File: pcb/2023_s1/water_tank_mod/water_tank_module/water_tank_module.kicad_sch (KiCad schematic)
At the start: 12 parts, among them J1 Conn_01x06_Male, U4 NRF24L01_Breakout

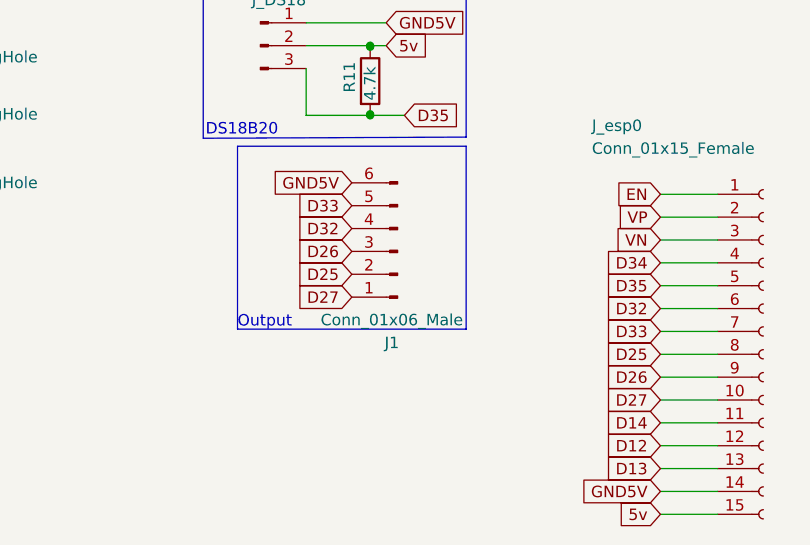
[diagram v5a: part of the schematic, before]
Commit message: fix, separated the light control into another pcb, due to the different voltage it handles and confort for the use
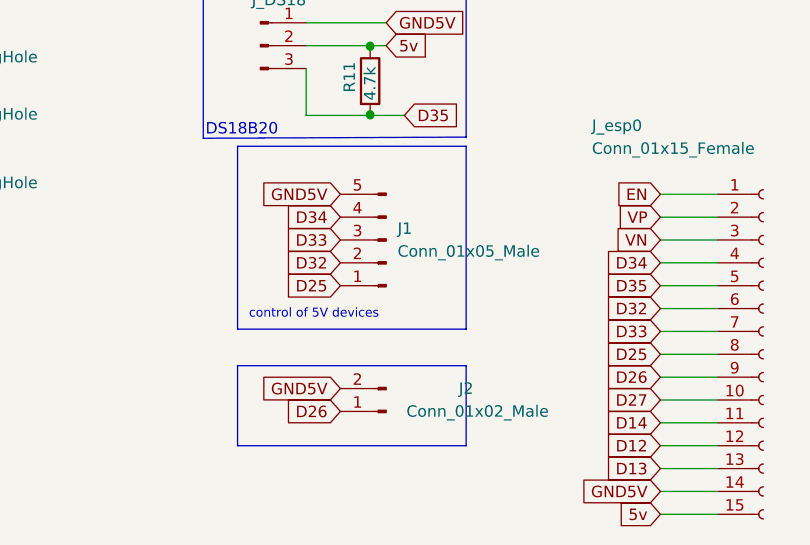
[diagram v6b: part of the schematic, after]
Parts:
- removed J1: Conn_01x06_Male, Connector_JST:JST_EH_B6B-EH-A_1x06_P2.50mm_Vertical, symbol Connector:Conn_01x06_Male
- added J1: Conn_01x05_Male, Connector_JST:JST_EH_B5B-EH-A_1x05_P2.50mm_Vertical, symbol Connector:Conn_01x05_Male
- added J2: Conn_01x02_Male, Connector_JST:JST_EH_B2B-EH-A_1x02_P2.50mm_Vertical, symbol Connector:Conn_01x02_Male
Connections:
- net D25: now also J1.1 (Pin_1)
- net D26: now also J2.1 (Pin_1)
- net D32: now also J1.2 (Pin_2)
- net D33: now also J1.3 (Pin_3)
- net D34: now also J1.4 (Pin_4)
- net GND5V: now also J1.5 (Pin_5), J2.2 (Pin_2)
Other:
- note added: "control of 5V devices"
- note removed: "Output"
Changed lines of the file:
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@@
+    (stroke (width 0) (type default) (color 0 0 0 0))
+  )
+  (polyline (pts (xy 76.2 88.9) (xy 101.6 88.9))
     (stroke (width 0) (type default) (color 0 0 0 0))
   )
@@
     (stroke (width 0) (type default) (color 0 0 0 0))
   )
+  (polyline (pts (xy 76.2 88.9) (xy 76.2 97.79))
+    (stroke (width 0) (type default) (color 0 0 0 0))
+  )
   (wire (pts (xy 123.19 100.33) (xy 129.54 100.33))
     (stroke (width 0) (type default) (color 0 0 0 0))
@@
     (stroke (width 0) (type default) (color 0 0 0 0))
   )
+  (polyline (pts (xy 101.6 88.9) (xy 101.6 97.79))
+    (stroke (width 0) (type default) (color 0 0 0 0))
+  )
   (wire (pts (xy 123.19 92.71) (xy 129.54 92.71))
     (stroke (width 0) (type default) (color 0 0 0 0))
@@
   )
   (wire (pts (xy 143.51 33.02) (xy 143.51 35.56))
+    (stroke (width 0) (type default) (color 0 0 0 0))
+  )
+  (polyline (pts (xy 101.6 97.79) (xy 76.2 97.79))
     (stroke (width 0) (type default) (color 0 0 0 0))
   )
@@
     (effects (font (size 1.27 1.27)) (justify left bottom))
   )
-  (text "Output" (at 76.2 84.836 0)
-    (effects (font (size 1.27 1.27)) (justify left bottom))
+  (text "control of 5V devices " (at 77.47 83.82 0)
+    (effects (font (size 1 1)) (justify left bottom))
   )
   (text "DS18B20" (at 72.644 63.5 0)
@@
     )
   )
-  (global_label "D26" (shape input) (at 88.9 76.2 180) (fields_autoplaced)
-    (effects (font (size 1.27 1.27)) (justify right))
-    (property "Intersheet References" "${INTERSHEET_REFS}" (id 0) (at 82.7979 76.1206 0)
-      (effects (font (size 1.27 1.27)) (justify right) hide)
-    )
-  )
   (global_label "D5" (shape input) (at 208.407 54.864 180) (fields_autoplaced)
     (effects (font (size 1.27 1.27)) (justify right))
@@
     )
   )
+  (global_label "D33" (shape input) (at 87.63 74.93 180) (fields_autoplaced)
+    (effects (font (size 1.27 1.27)) (justify right))
+    (property "Intersheet References" "${INTERSHEET_REFS}" (id 0) (at 81.5279 75.0094 0)
+      (effects (font (size 1.27 1.27)) (justify right) hide)
+    )
+  )
   (global_label "GND5V" (shape input) (at 221.107 70.104 270) (fields_autoplaced)
     (effects (font (size 1.27 1.27)) (justify right))
@@
     )
   )
+  (global_label "GND5V" (shape input) (at 87.63 91.44 180) (fields_autoplaced)
+    (effects (font (size 1.27 1.27)) (justify right))
+    (property "Intersheet References" "${INTERSHEET_REFS}" (id 0) (at 79.0483 91.5194 0)
+      (effects (font (size 1.27 1.27)) (justify right) hide)
+    )
+  )
   (global_label "D34" (shape input) (at 123.19 77.47 180) (fields_autoplaced)
     (effects (font (size 1.27 1.27)) (justify right))
@@
     )
   )
+  (global_label "GND5V" (shape input) (at 87.63 69.85 180) (fields_autoplaced)
+    (effects (font (size 1.27 1.27)) (justify right))
+    (property "Intersheet References" "${INTERSHEET_REFS}" (id 0) (at 79.0483 69.9294 0)
+      (effects (font (size 1.27 1.27)) (justify right) hide)
+    )
+  )
   (global_label "D27" (shape input) (at 123.19 92.71 180) (fields_autoplaced)
     (effects (font (size 1.27 1.27)) (justify right))
@@
     )
   )
+  (global_label "D25" (shape input) (at 87.63 80.01 180) (fields_autoplaced)
+    (effects (font (size 1.27 1.27)) (justify right))
+    (property "Intersheet References" "${INTERSHEET_REFS}" (id 0) (at 81.5279 79.9306 0)
+      (effects (font (size 1.27 1.27)) (justify right) hide)
+    )
+  )
   (global_label "D14" (shape input) (at 123.19 95.25 180) (fields_autoplaced)
     (effects (font (size 1.27 1.27)) (justify right))
@@
     )
   )
-  (global_label "GND5V" (shape input) (at 88.9 68.58 180) (fields_autoplaced)
-    (effects (font (size 1.27 1.27)) (justify right))
-    (property "Intersheet References" "${INTERSHEET_REFS}" (id 0) (at 80.3183 68.6594 0)
-      (effects (font (size 1.27 1.27)) (justify right) hide)
-    )
-  )
   (global_label "D21" (shape input) (at 167.64 80.01 0) (fields_autoplaced)
     (effects (font (size 1.27 1.27)) (justify left))
@@
     )
   )
+  (global_label "D32" (shape input) (at 87.63 77.47 180) (fields_autoplaced)
+    (effects (font (size 1.27 1.27)) (justify right))
+    (property "Intersheet References" "${INTERSHEET_REFS}" (id 0) (at 81.5279 77.3906 0)
+      (effects (font (size 1.27 1.27)) (justify right) hide)
+    )
+  )
   (global_label "VN" (shape input) (at 123.19 74.93 180) (fields_autoplaced)
     (effects (font (size 1.27 1.27)) (justify right))
@@
     )
   )
-  (global_label "D33" (shape input) (at 88.9 71.12 180) (fields_autoplaced)
-    (effects (font (size 1.27 1.27)) (justify right))
-    (property "Intersheet References" "${INTERSHEET_REFS}" (id 0) (at 82.7979 71.1994 0)
-      (effects (font (size 1.27 1.27)) (justify right) hide)
-    )
-  )
   (global_label "D12" (shape input) (at 123.19 97.79 180) (fields_autoplaced)
     (effects (font (size 1.27 1.27)) (justify right))
@@
     )
   )
-  (global_label "D25" (shape input) (at 88.9 78.74 180) (fields_autoplaced)
-    (effects (font (size 1.27 1.27)) (justify right))
-    (property "Intersheet References" "${INTERSHEET_REFS}" (id 0) (at 82.7979 78.6606 0)
-      (effects (font (size 1.27 1.27)) (justify right) hide)
-    )
-  )
   (global_label "D23" (shape input) (at 167.64 69.85 0) (fields_autoplaced)
     (effects (font (size 1.27 1.27)) (justify left))
@@
     )
   )
-  (global_label "D27" (shape input) (at 88.9 81.28 180) (fields_autoplaced)
-    (effects (font (size 1.27 1.27)) (justify right))
-    (property "Intersheet References" "${INTERSHEET_REFS}" (id 0) (at 82.7979 81.2006 0)
+  (global_label "D26" (shape input) (at 87.63 93.98 180) (fields_autoplaced)
+    (effects (font (size 1.27 1.27)) (justify right))
+    (property "Intersheet References" "${INTERSHEET_REFS}" (id 0) (at 81.5279 93.9006 0)
       (effects (font (size 1.27 1.27)) (justify right) hide)
     )
@@
     )
   )
+  (global_label "D34" (shape input) (at 87.63 72.39 180) (fields_autoplaced)
+    (effects (font (size 1.27 1.27)) (justify right))
+    (property "Intersheet References" "${INTERSHEET_REFS}" (id 0) (at 81.5279 72.3106 0)
+      (effects (font (size 1.27 1.27)) (justify right) hide)
+    )
+  )
   (global_label "D23" (shape input) (at 208.407 47.244 180) (fields_autoplaced)
     (effects (font (size 1.27 1.27)) (justify right))
@@
     )
   )
-  (global_label "D32" (shape input) (at 88.9 73.66 180) (fields_autoplaced)
-    (effects (font (size 1.27 1.27)) (justify right))
-    (property "Intersheet References" "${INTERSHEET_REFS}" (id 0) (at 82.7979 73.5806 0)
-      (effects (font (size 1.27 1.27)) (justify right) hide)
-    )
-  )
   (global_label "D19" (shape input) (at 167.64 82.55 0) (fields_autoplaced)
     (effects (font (size 1.27 1.27)) (justify left))
@@
     )
   )
-  (symbol (lib_id "Connector:Conn_01x06_Male") (at 93.98 76.2 180) (unit 1)
+  (symbol (lib_id "Connector:Conn_01x05_Male") (at 92.71 74.93 180) (unit 1)
     (in_bom yes) (on_board yes) (fields_autoplaced)
-    (property "Reference" "J1" (id 0) (at 93.345 86.36 0))
-    (property "Value" "Conn_01x06_Male" (id 1) (at 93.345 83.82 0))
-    (property "Footprint" "Connector_JST:JST_EH_B6B-EH-A_1x06_P2.50mm_Vertical" (id 2) (at 93.98 76.2 0)
-      (effects (font (size 1.27 1.27)) hide)
-    )
-    (property "Datasheet" "~" (id 3) (at 93.98 76.2 0)
+    (property "Reference" "J1" (id 0) (at 93.98 73.6599 0)
+      (effects (font (size 1.27 1.27)) (justify right))
+    )
+    (property "Value" "Conn_01x05_Male" (id 1) (at 93.98 76.1999 0)
+      (effects (font (size 1.27 1.27)) (justify right))
+    )
+    (property "Footprint" "Connector_JST:JST_EH_B5B-EH-A_1x05_P2.50mm_Vertical" (id 2) (at 92.71 74.93 0)
+      (effects (font (size 1.27 1.27)) hide)
+    )
+    (property "Datasheet" "~" (id 3) (at 92.71 74.93 0)
       (effects (font (size 1.27 1.27)) hide)
     )
@@
     (pin "4")
     (pin "5")
-    (pin "6")
   )
   (symbol (lib_id "Connector:Conn_01x03_Male") (at 82.55 38.481 0) (unit 1)
@@
     (pin "9")
   )
+  (symbol (lib_id "Connector:Conn_01x02_Male") (at 92.71 93.98 180) (unit 1)
+    (in_bom yes) (on_board yes)
+    (property "Reference" "J2" (id 0) (at 101.6 91.44 0))
+    (property "Value" "Conn_01x02_Male" (id 1) (at 102.87 93.98 0))
+    (property "Footprint" "Connector_JST:JST_EH_B2B-EH-A_1x02_P2.50mm_Vertical" (id 2) (at 92.71 93.98 0)
+      (effects (font (size 1.27 1.27)) hide)
+    )
+    (property "Datasheet" "~" (id 3) (at 92.71 93.98 0)
+      (effects (font (size 1.27 1.27)) hide)
+    )
+    (pin "1")
+    (pin "2")
+  )
   (symbol (lib_id "Mechanical:MountingHole") (at 39.37 67.31 0) (unit 1)
     (in_bom yes) (on_board yes) (fields_autoplaced)
@@
       (reference "H3") (unit 1) (value "MountingHole") (footprint "MountingHole:MountingHole_2.7mm_M2.5_Pad")
     )
-    (path "/05f4494b-5779-46e5-8ae9-0f5ec633c154"
-      (reference "J1") (unit 1) (value "Conn_01x06_Male") (footprint "Connector_JST:JST_EH_B6B-EH-A_1x06_P2.50mm_Vertical")
+    (path "/0acd31bd-0a92-415d-b1ae-b860cc8ad816"
+      (reference "J1") (unit 1) (value "Conn_01x05_Male") (footprint "Connector_JST:JST_EH_B5B-EH-A_1x05_P2.50mm_Vertical")
+    )
+    (path "/e9985b2b-95c9-4d1b-aa33-6bba12cffcb1"
+      (reference "J2") (unit 1) (value "Conn_01x02_Male") (footprint "Connector_JST:JST_EH_B2B-EH-A_1x02_P2.50mm_Vertical")
     )
     (path "/977a8c43-25e0-4675-a166-3f6d7cf1e985"
